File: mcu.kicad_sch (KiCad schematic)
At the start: 32 parts, among them IC2 STM32H723ZGT6, J1 Conn_ST_STDC14, SW1 RESET, Y1 16MHz

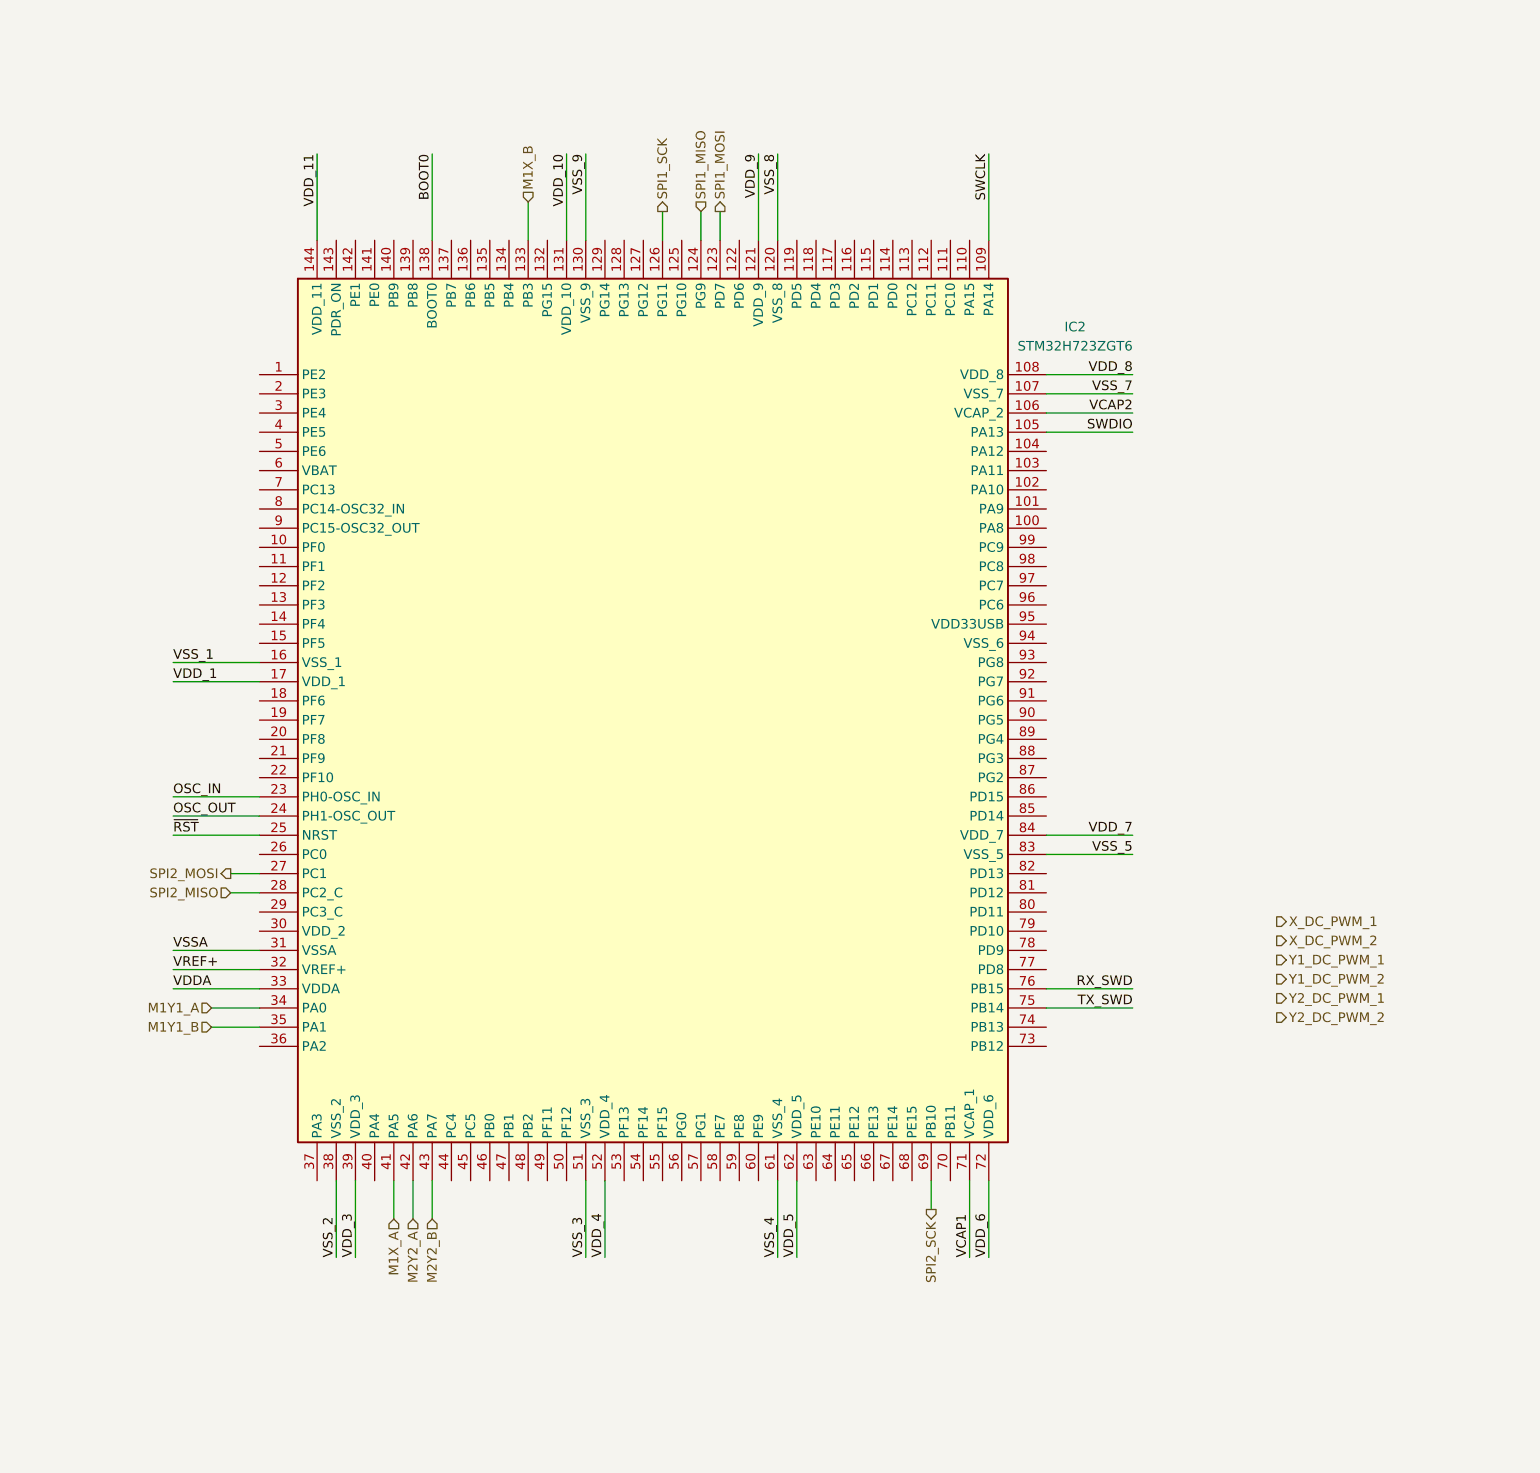
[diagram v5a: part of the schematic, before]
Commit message: feat: pwms for DC motors
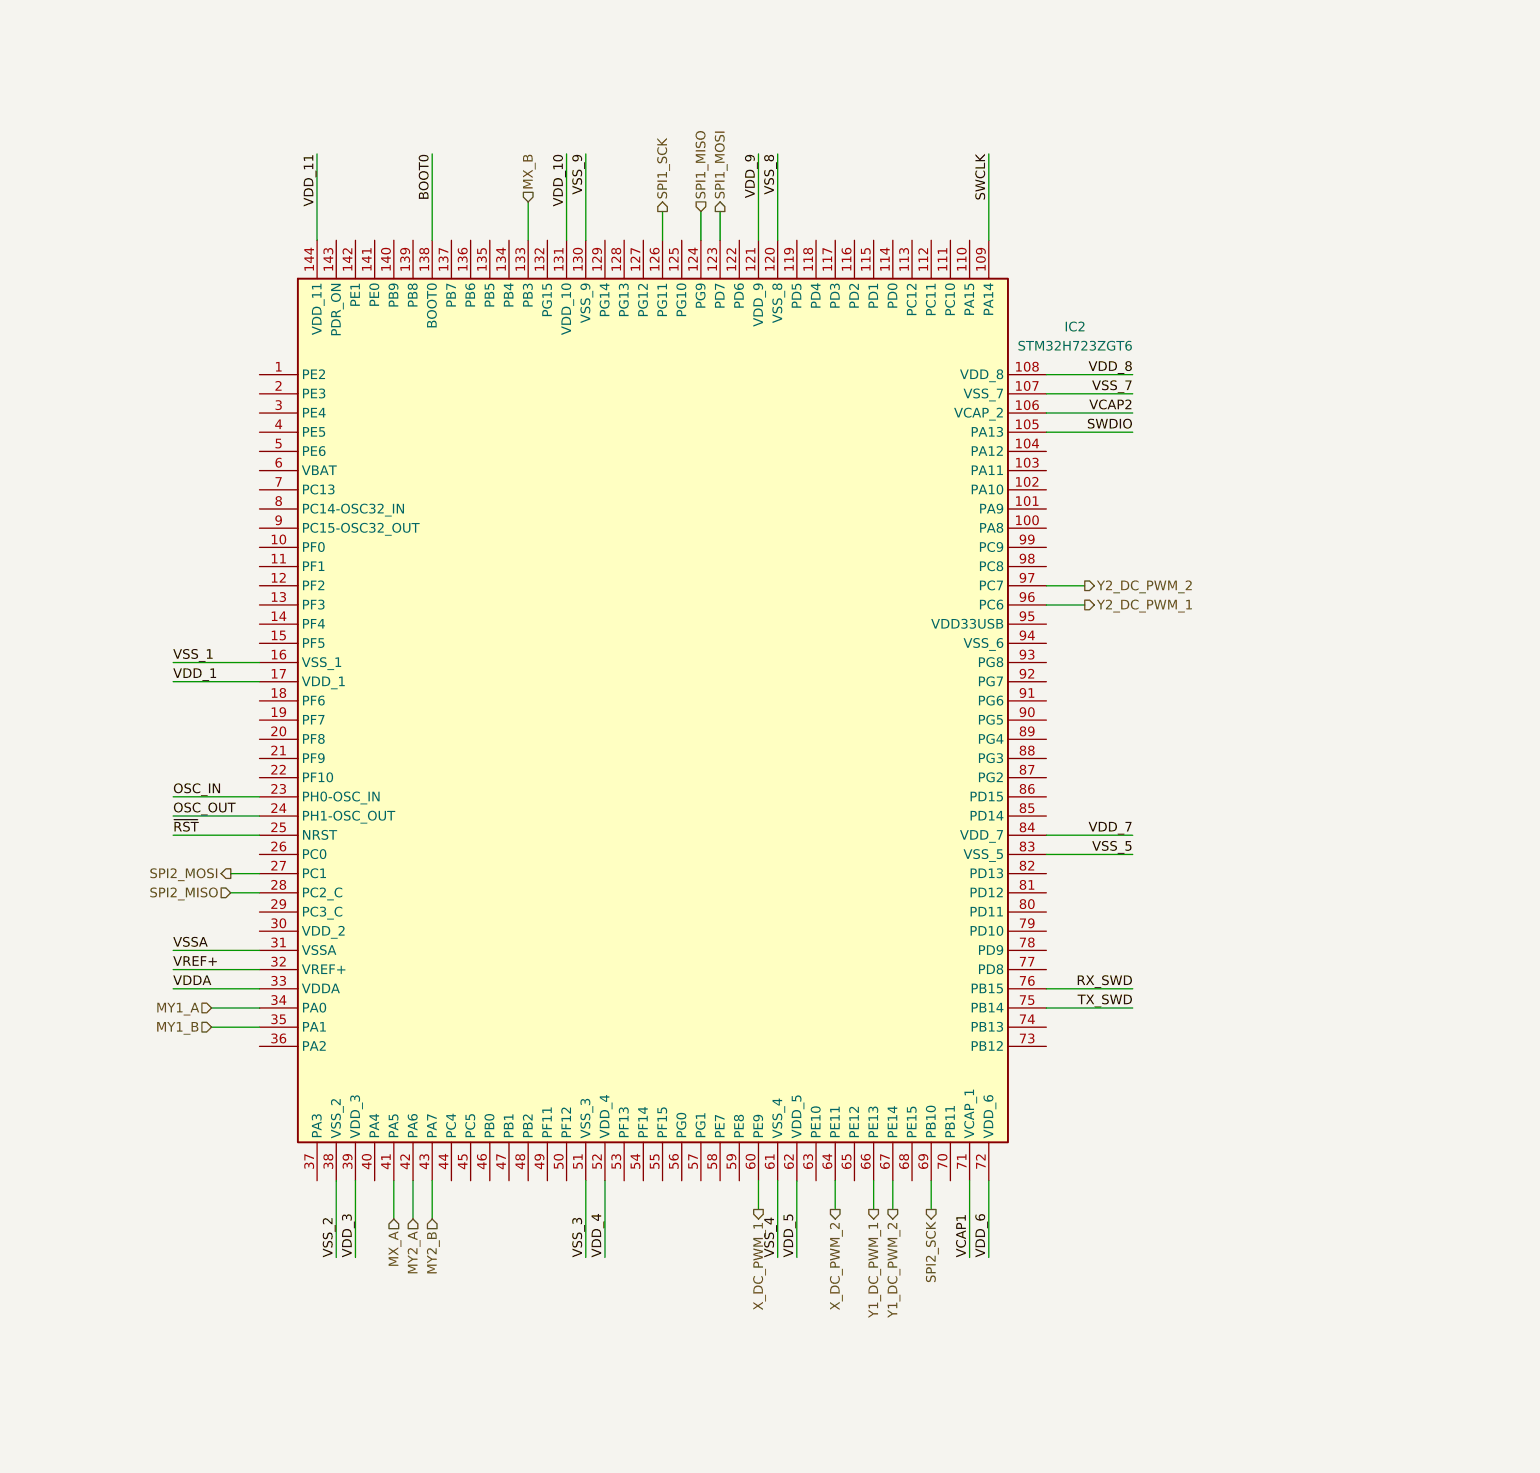
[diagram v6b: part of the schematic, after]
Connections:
- net X_DC_PWM_1: now also IC2.60 (PE9)
- net X_DC_PWM_2: now also IC2.64 (PE11)
- net Y1_DC_PWM_1: now also IC2.66 (PE13)
- net Y1_DC_PWM_2: now also IC2.67 (PE14)
- net Y2_DC_PWM_1: now also IC2.96 (PC6)
- net Y2_DC_PWM_2: now also IC2.97 (PC7)
- net M1X_A renamed MX_A
- net M1X_B renamed MX_B
- net M1Y1_A renamed MY1_A
- net M1Y1_B renamed MY1_B
- net M2Y2_A renamed MY2_A
- net M2Y2_B renamed MY2_B
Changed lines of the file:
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@@
+		)
+	)
+	(wire
+		(pts
+			(xy 223.52 204.47) (xy 223.52 208.28)
+		)
+		(stroke
+			(width 0)
+			(type default)
 		)
 	)
@@
 	(wire
 		(pts
+			(xy 261.62 128.27) (xy 266.7 128.27)
+		)
+		(stroke
+			(width 0)
+			(type default)
+		)
+	)
+	(wire
+		(pts
 			(xy 27.94 95.25) (xy 31.75 95.25)
 		)
@@
 	(wire
 		(pts
+			(xy 238.76 204.47) (xy 238.76 208.28)
+		)
+		(stroke
+			(width 0)
+			(type default)
+		)
+	)
+	(wire
+		(pts
 			(xy 261.62 158.75) (xy 273.05 158.75)
 		)
@@
 	(wire
 		(pts
+			(xy 241.3 204.47) (xy 241.3 208.28)
+		)
+		(stroke
+			(width 0)
+			(type default)
+		)
+	)
+	(wire
+		(pts
 			(xy 67.31 199.39) (xy 67.31 198.12)
 		)
@@
 	(wire
 		(pts
+			(xy 233.68 204.47) (xy 233.68 208.28)
+		)
+		(stroke
+			(width 0)
+			(type default)
+		)
+	)
+	(wire
+		(pts
 			(xy 91.44 127) (xy 82.55 127)
+		)
+		(stroke
+			(width 0)
+			(type default)
+		)
+	)
+	(wire
+		(pts
+			(xy 261.62 125.73) (xy 266.7 125.73)
 		)
 		(stroke
@@
 	(hierarchical_label "X_DC_PWM_1"
 		(shape output)
-		(at 292.1 170.18 0)
-		(effects
-			(font
-				(size 1.27 1.27)
-			)
-			(justify left)
+		(at 223.52 208.28 270)
+		(effects
+			(font
+				(size 1.27 1.27)
+			)
+			(justify right)
 		)
 	)
@@
 		)
 	)
-	(hierarchical_label "M2Y2_A"
+	(hierarchical_label "MY2_A"
 		(shape input)
 		(at 177.8 209.55 270)
@@
 		)
 	)
-	(hierarchical_label "M1X_B"
+	(hierarchical_label "MX_B"
 		(shape input)
 		(at 193.04 74.93 90)
@@
 	(hierarchical_label "X_DC_PWM_2"
 		(shape output)
-		(at 292.1 172.72 0)
-		(effects
-			(font
-				(size 1.27 1.27)
-			)
-			(justify left)
-		)
-	)
-	(hierarchical_label "M1X_A"
+		(at 233.68 208.28 270)
+		(effects
+			(font
+				(size 1.27 1.27)
+			)
+			(justify right)
+		)
+	)
+	(hierarchical_label "MX_A"
 		(shape input)
 		(at 175.26 209.55 270)
@@
 	(hierarchical_label "Y1_DC_PWM_2"
 		(shape output)
-		(at 292.1 177.8 0)
-		(effects
-			(font
-				(size 1.27 1.27)
-			)
-			(justify left)
+		(at 241.3 208.28 270)
+		(effects
+			(font
+				(size 1.27 1.27)
+			)
+			(justify right)
 		)
 	)
@@
 	(hierarchical_label "Y2_DC_PWM_1"
 		(shape output)
-		(at 292.1 180.34 0)
+		(at 266.7 128.27 0)
 		(effects
 			(font
@@
 		)
 	)
-	(hierarchical_label "M1Y1_B"
+	(hierarchical_label "MY1_B"
 		(shape input)
 		(at 151.13 184.15 180)
@@
 	(hierarchical_label "Y2_DC_PWM_2"
 		(shape output)
-		(at 292.1 182.88 0)
+		(at 266.7 125.73 0)
 		(effects
 			(font
@@
 		)
 	)
-	(hierarchical_label "M1Y1_A"
+	(hierarchical_label "MY1_A"
 		(shape input)
 		(at 151.13 181.61 180)
@@
 	(hierarchical_label "Y1_DC_PWM_1"
 		(shape output)
-		(at 292.1 175.26 0)
-		(effects
-			(font
-				(size 1.27 1.27)
-			)
-			(justify left)
-		)
-	)
-	(hierarchical_label "M2Y2_B"
+		(at 238.76 208.28 270)
+		(effects
+			(font
+				(size 1.27 1.27)
+			)
+			(justify right)
+		)
+	)
+	(hierarchical_label "MY2_B"
 		(shape input)
 		(at 180.34 209.55 270)

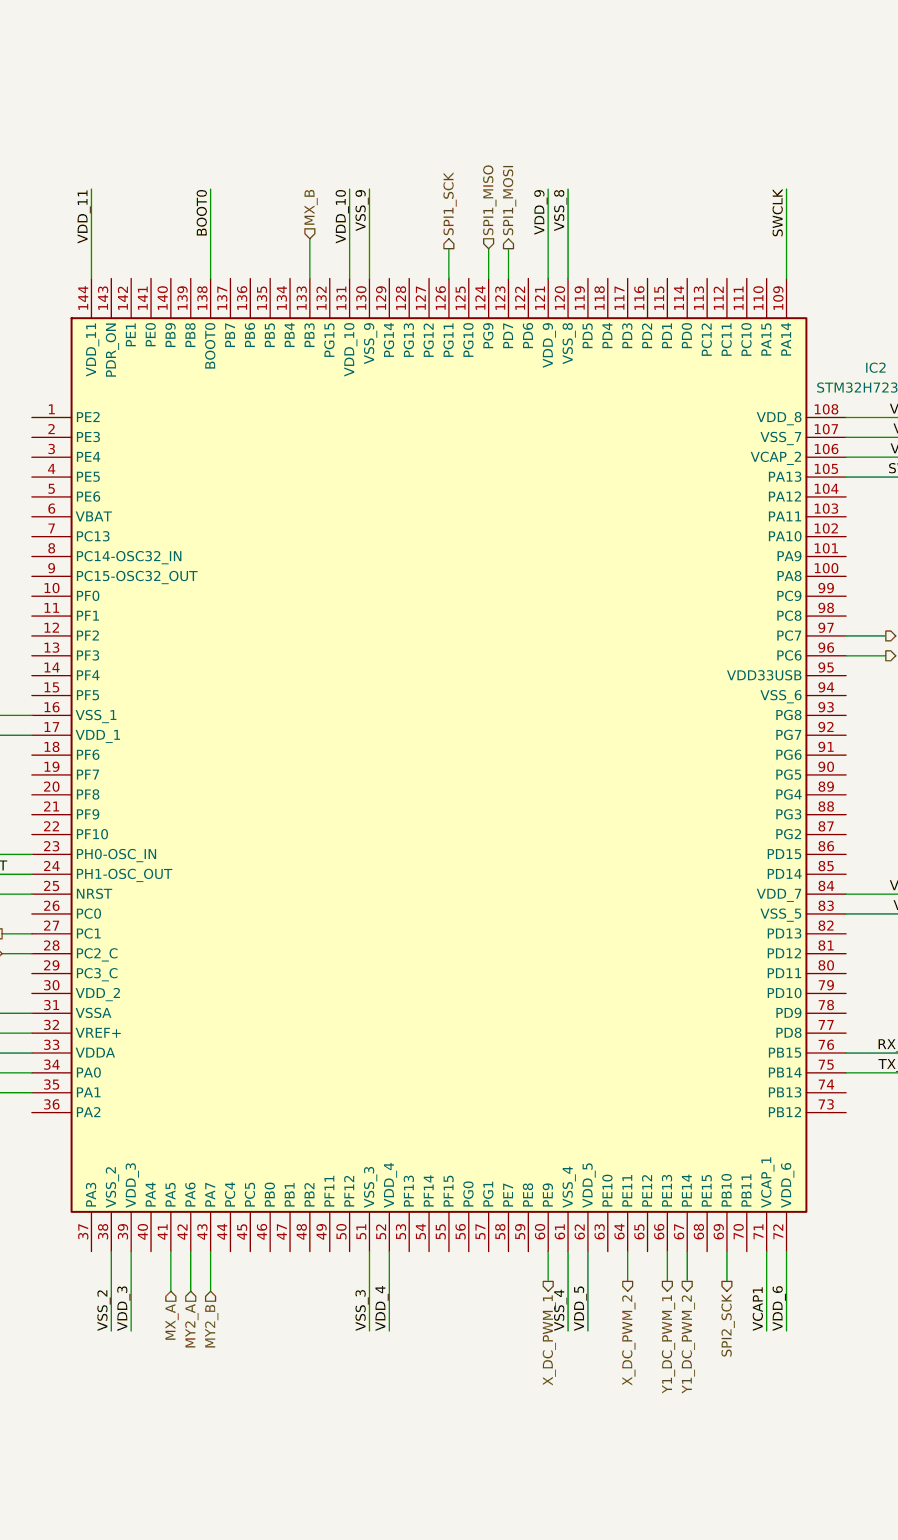
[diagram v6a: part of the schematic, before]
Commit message: feat: raspberry spi dma setup and footprints fix
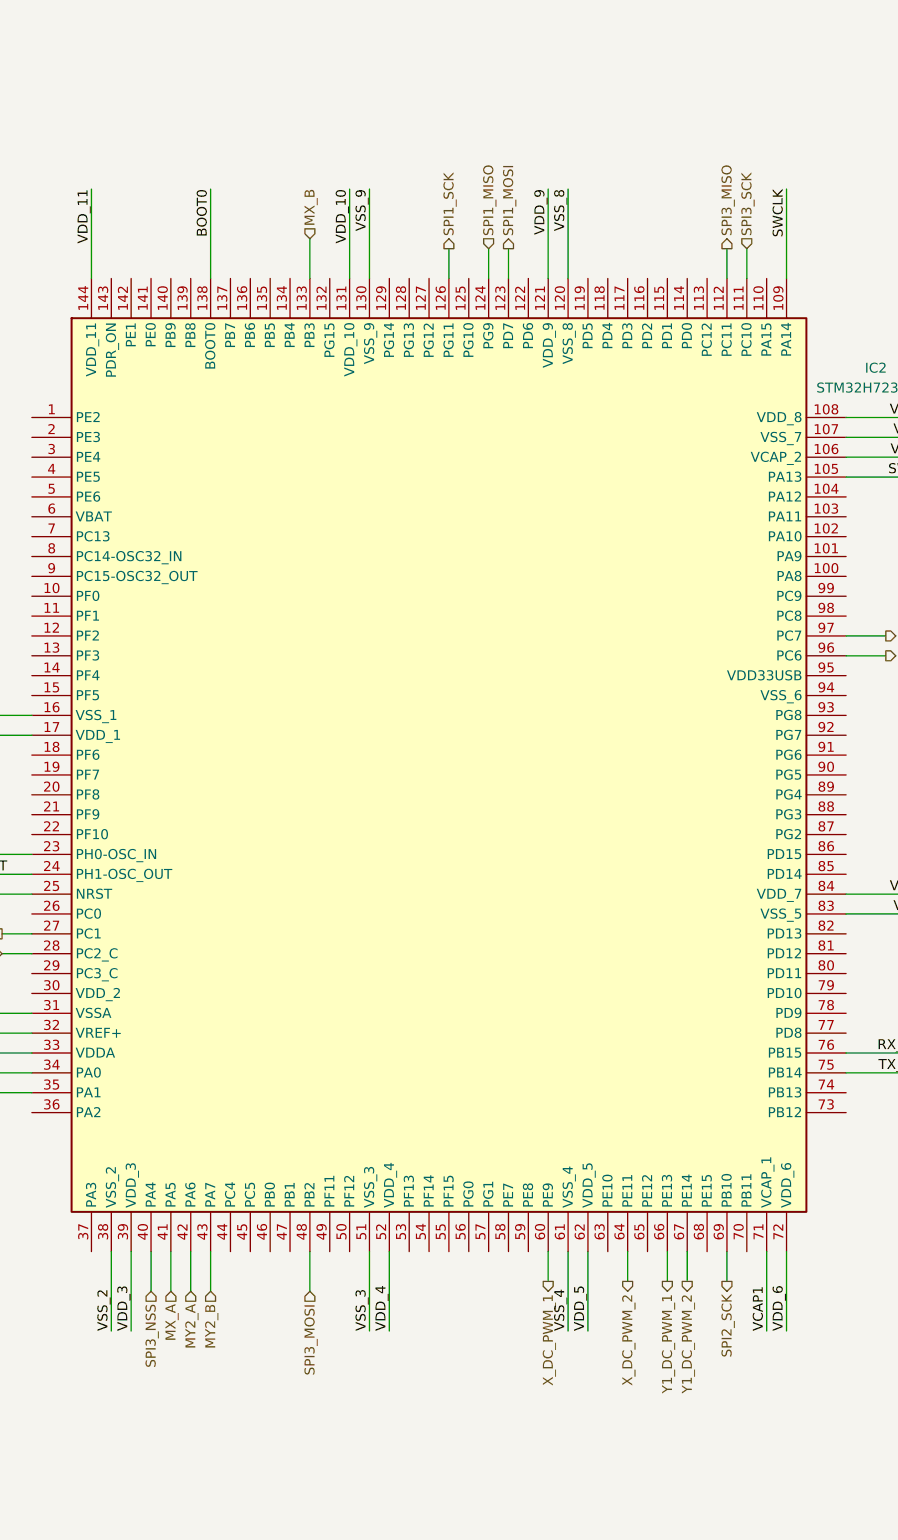
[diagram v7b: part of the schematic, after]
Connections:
- net SPI3_SCK: now reaches IC2.111 (PC10)
- net SPI3_MISO: now reaches IC2.112 (PC11)
- net SPI3_NSS: now reaches IC2.40 (PA4)
- net SPI3_MOSI: now reaches IC2.48 (PB2)
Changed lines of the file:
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@@
+	(wire
+		(pts
+			(xy 248.92 76.2) (xy 248.92 80.01)
+		)
+		(stroke
+			(width 0)
+			(type default)
+		)
+	)
 	(wire
 		(pts
@@
 	(wire
 		(pts
+			(xy 246.38 76.2) (xy 246.38 80.01)
+		)
+		(stroke
+			(width 0)
+			(type default)
+		)
+	)
+	(wire
+		(pts
 			(xy 73.66 66.04) (xy 73.66 67.31)
 		)
@@
 		)
 	)
+	(wire
+		(pts
+			(xy 172.72 204.47) (xy 172.72 209.55)
+		)
+		(stroke
+			(width 0)
+			(type default)
+		)
+	)
 	(polyline
 		(pts
@@
 		(pts
 			(xy 22.86 134.62) (xy 38.1 134.62)
+		)
+		(stroke
+			(width 0)
+			(type default)
+		)
+	)
+	(wire
+		(pts
+			(xy 193.04 204.47) (xy 193.04 209.55)
 		)
 		(stroke
@@
 		)
 	)
+	(hierarchical_label "SPI3_MOSI"
+		(shape input)
+		(at 193.04 209.55 270)
+		(effects
+			(font
+				(size 1.27 1.27)
+			)
+			(justify right)
+		)
+	)
 	(hierarchical_label "MY2_A"
 		(shape input)
@@
 		)
 	)
+	(hierarchical_label "SPI3_MISO"
+		(shape output)
+		(at 246.38 76.2 90)
+		(effects
+			(font
+				(size 1.27 1.27)
+			)
+			(justify left)
+		)
+	)
 	(hierarchical_label "MX_B"
 		(shape input)
@@
 		)
 	)
+	(hierarchical_label "SPI3_NSS"
+		(shape input)
+		(at 172.72 209.55 270)
+		(effects
+			(font
+				(size 1.27 1.27)
+			)
+			(justify right)
+		)
+	)
 	(hierarchical_label "SPI2_SCK"
 		(shape output)
@@
 		)
 	)
+	(hierarchical_label "SPI3_SCK"
+		(shape input)
+		(at 248.92 76.2 90)
+		(effects
+			(font
+				(size 1.27 1.27)
+			)
+			(justify left)
+		)
+	)

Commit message: fix: missing decoupling caps
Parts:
- added C57, C59: 100n, Capacitor_SMD:C_0603_1608Metric, symbol Device:C
- added C58: 1u, Capacitor_SMD:C_0805_2012Metric, symbol Device:C
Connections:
- net +3V3: now also IC2.30 (VDD_2), IC2.6 (VBAT), IC2.95 (VDD33USB), C57.1, C58.1, C59.1
- net GND: now also C57.2, C58.2, C59.2
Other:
- note added: "USB"
- moved on the sheet: C24, C25, C26
